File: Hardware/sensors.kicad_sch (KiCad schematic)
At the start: 32 parts, among them IC1 BMP388, IC2 ICM-42688-P, J1 Conn_Coaxial, J12 Conn_Coaxial, Q1 BC847B, Q2 BC847B, U2 MAX-M10S

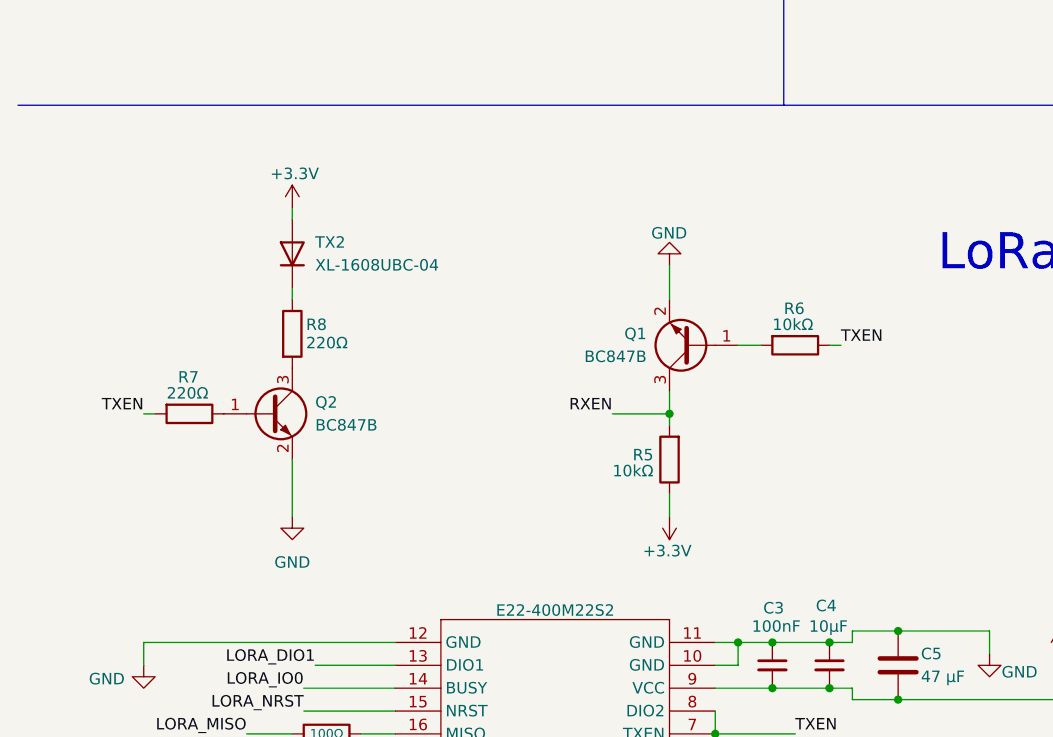
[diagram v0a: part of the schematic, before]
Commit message: Power sch added
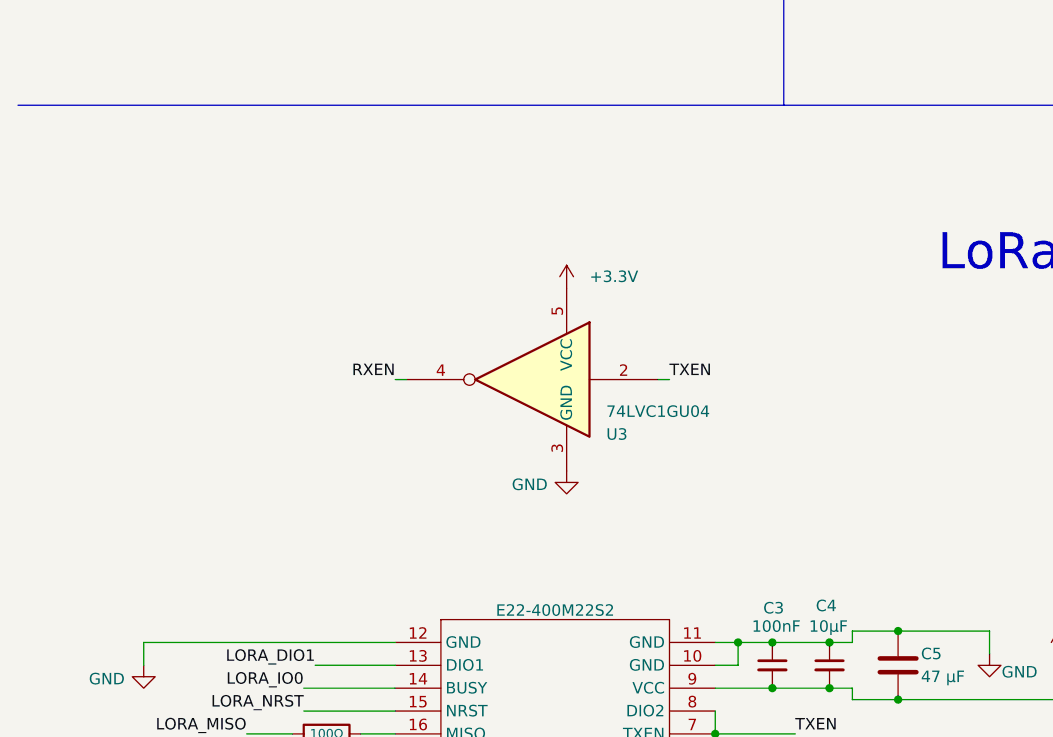
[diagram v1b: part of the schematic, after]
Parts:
- removed Q1, Q2: BC847B, Package_TO_SOT_SMD:SOT-23, symbol Transistor_BJT:BC847
- removed R5, R6: 10kΩ, Resistor_SMD:R_0402_1005Metric, symbol Device:R
- removed R7, R8: 220Ω, Resistor_SMD:R_0402_1005Metric, symbol Device:R
- removed TX2: XL-1608UBC-04, LED_SMD:LED_0603_1608Metric, symbol Diode:1SS355VM
- added U3: 74LVC1GU04, symbol 74xGxx:74LVC1GU04
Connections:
- net +3.3V: now also U3.5 (VCC)
- net GND: now also U3.3 (GND)
- net RXEN: now also U3.4
- net TXEN: now also U3.2
